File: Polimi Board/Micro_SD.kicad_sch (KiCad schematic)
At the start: 7 parts, among them J3 Micro_SD_Card, U4 74LVC125, U5 74LVC125

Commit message: Finish schematic part
To be reviewd
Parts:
- removed U5: 74LVC125, symbol 74xx:74LVC125
- added unit 2 of U4
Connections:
- net GND: now also U4.4; no longer J3.9 (SHIELD)
- net SCK_LLS: now also U4.6
- net at R8.2: now also U4.5
- new net Earth: J3.9 (SHIELD)

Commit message: Fatte modifiche
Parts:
- removed J3: Micro_SD_Card, symbol Connector:Micro_SD_Card
- removed U4: 74LVC125, symbol 74xx:74LVC125
- added J7: SD_Card, symbol Connector:SD_Card
- added R33, R34, R35: 47k, symbol Device:R
- R10, R7, R8, R9: value 3.3K -> 47k
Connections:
- net CS is gone; now on net +3.3V: R9.1
- net MISO is gone; now on net +3.3V: R10.1
- net MOSI is gone; now on net +3.3V: R7.1
- net SCK is gone; now on net +3.3V: R8.1
- net +3.3V: now also J7.4 (VDD), R33.1, R34.1, R35.1
- net GND: now also J7.12 (SHELL1), J7.13 (SHELL2), J7.3 (VSS), J7.6 (VSS)
- net SDMMC_D2: now reaches R7.2
- net SDMMC_D2: now also J7.9 (DAT2)
- net SDMMC_D0: now reaches R10.2
- net SDMMC_D0: now also J7.7 (DAT0)
- net SDMMC_D3: now reaches R8.2
- net SDMMC_D3: now also J7.1 (CD/DAT3)
- net SDMMC_CMD: now reaches R9.2
- net SDMMC_CMD: now also J7.2 (CMD)
- new net SDMMC_CD: J7.10 (CARD_DETECT), R34.2
- new net SDMMC_CK: J7.5 (CLK)
- new net SDMMC_D1: J7.8 (DAT1), R33.2
- new net SDMMC_WP: J7.11 (WRITE_PROTECT), R35.2
- no-connect marks 2 -> 0
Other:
- note removed: "Level shifter"

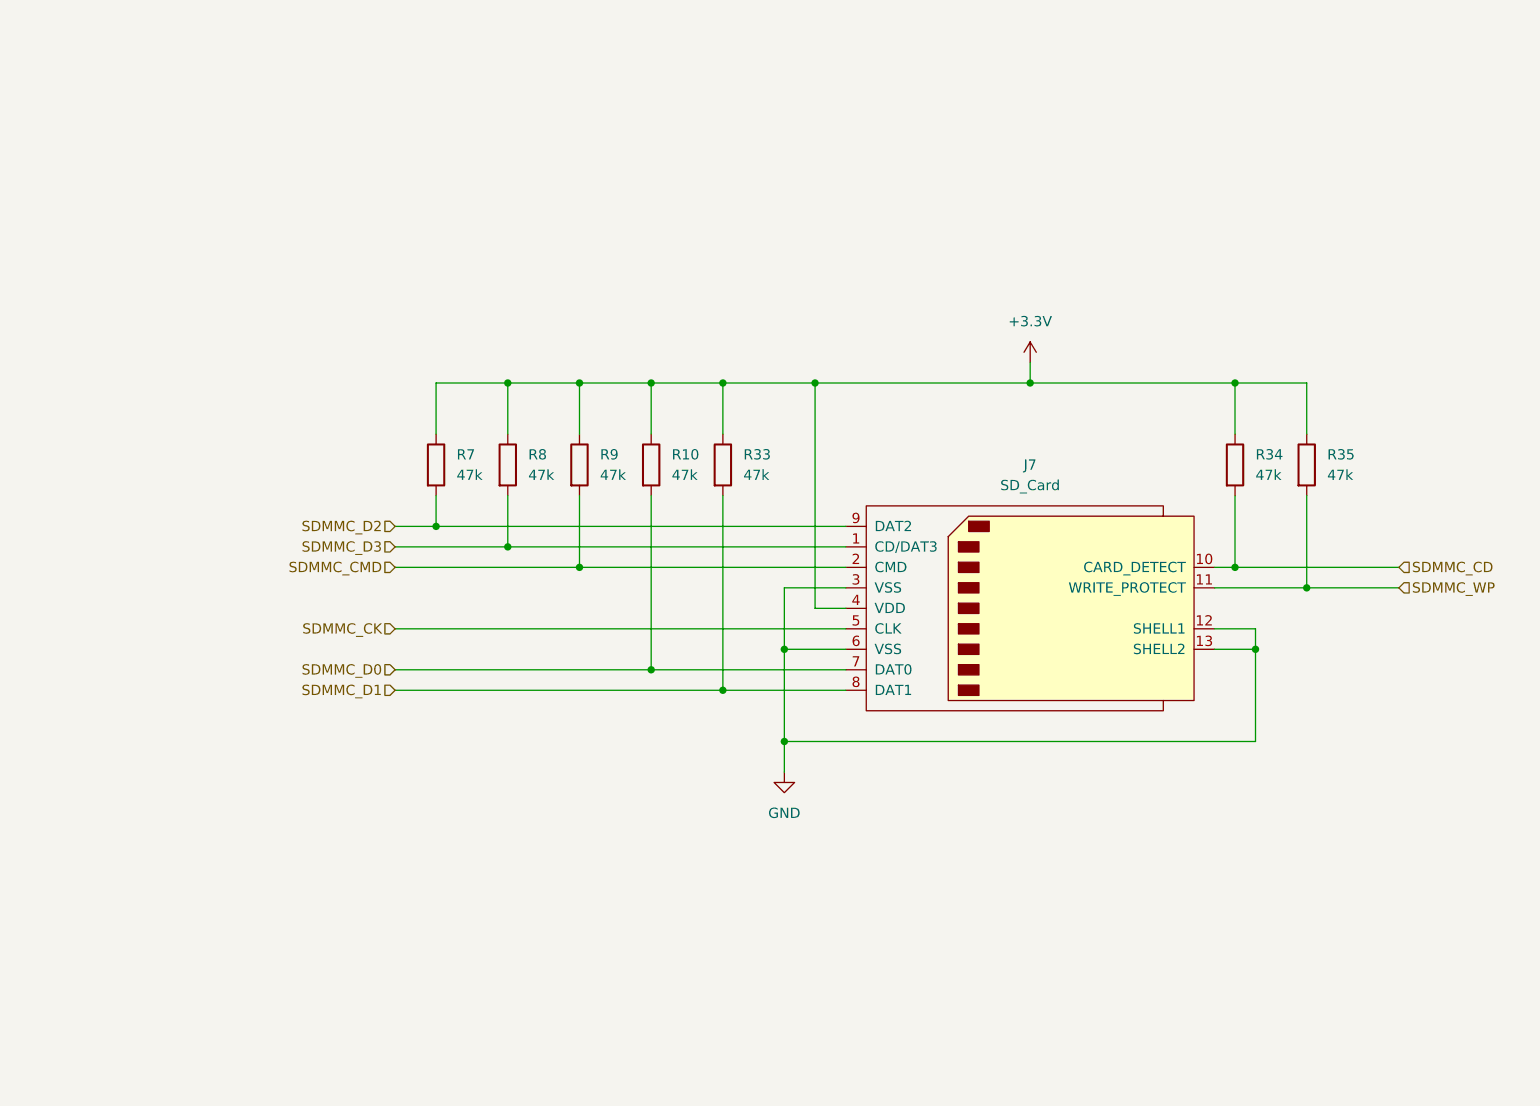
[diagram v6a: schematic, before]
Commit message: Added footprint from Mouser
readu for wiring
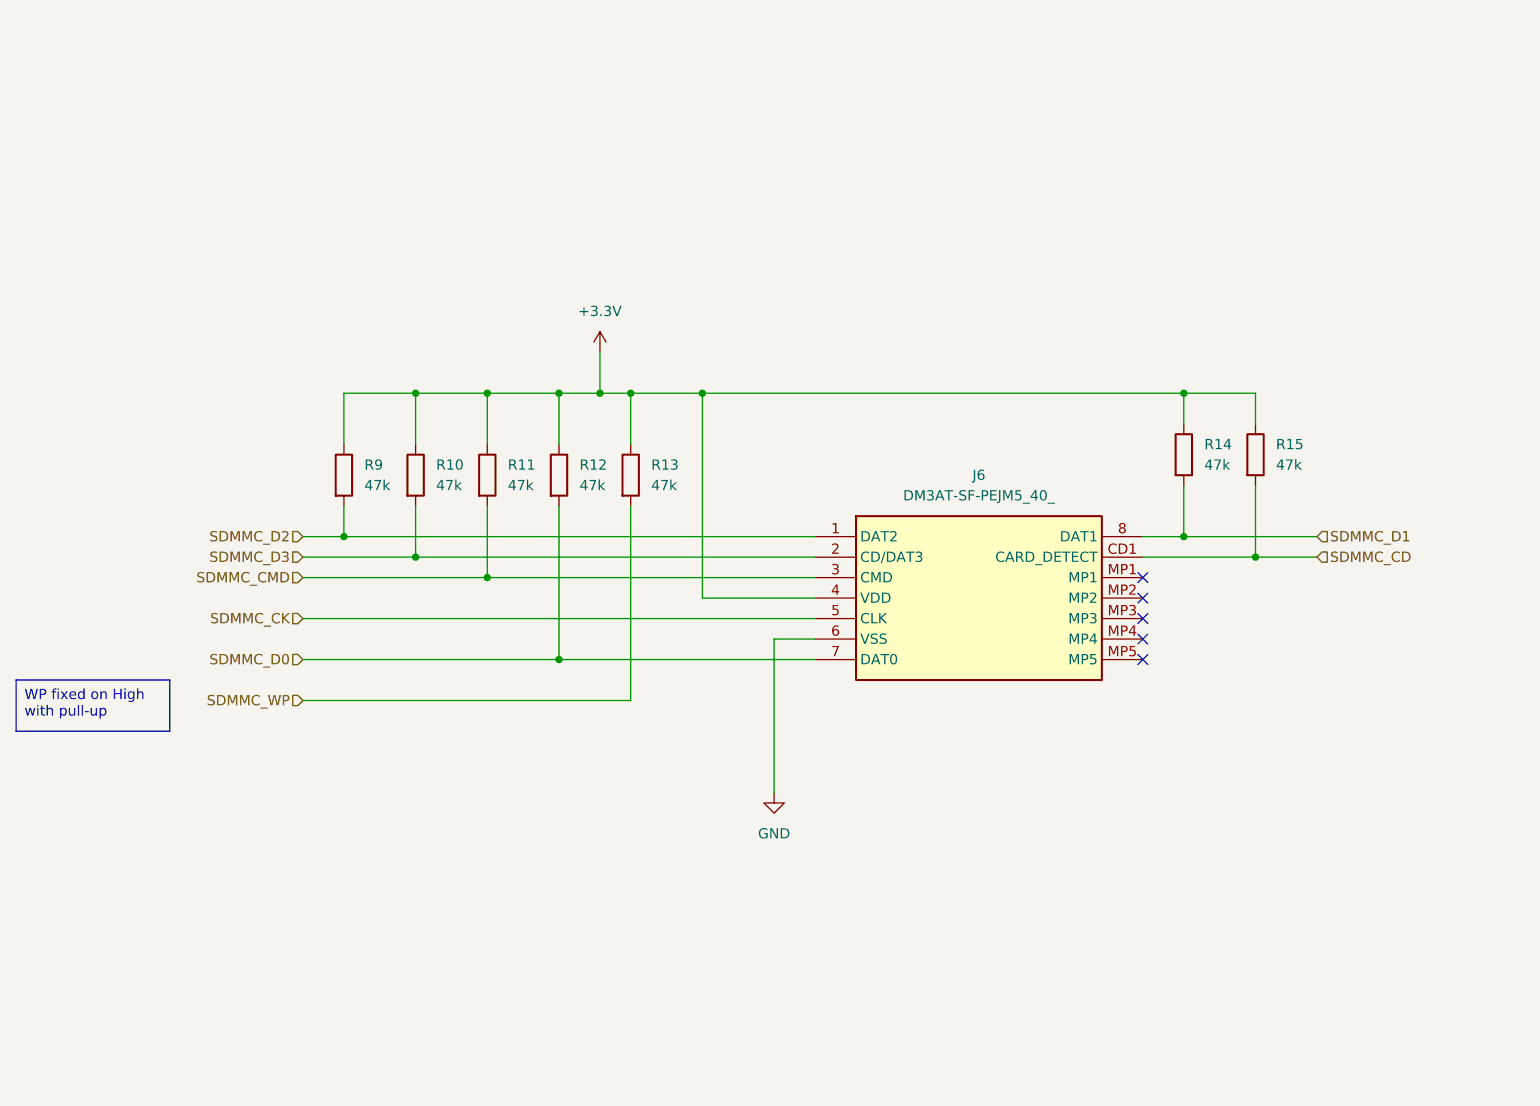
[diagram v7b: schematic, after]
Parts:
- removed J7: SD_Card, symbol Connector:SD_Card
- removed R33, R34, R35, R7, R8: 47k, symbol Device:R
- added J6: DM3AT-SF-PEJM5_40_, SamacSys_Parts:DM3ATSFPEJM540, symbol SamacSys_Parts:DM3AT-SF-PEJM5_40_
- added R11, R12, R13, R14, R15: 47k, Resistor_SMD:R_0603_1608Metric_Pad0.98x0.95mm_HandSolder, symbol Device:R
- R10, R9: footprint (none) -> Resistor_SMD:R_0603_1608Metric_Pad0.98x0.95mm_HandSolder
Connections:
- net +3.3V: now also J6.4 (VDD), R11.1, R12.1, R13.1, R14.1, R15.1
- net GND: now also J6.6 (VSS)
- net SDMMC_CD: now also J6.CD1 (CARD_DETECT), R15.2
- net SDMMC_CK: now also J6.5 (CLK)
- net SDMMC_CMD: now also J6.3 (CMD), R11.2; no longer R9.2
- net SDMMC_D0: now also J6.7 (DAT0), R12.2; no longer R10.2
- net SDMMC_D1: now also J6.8 (DAT1), R14.2
- net SDMMC_D2: now also R9.2, J6.1 (DAT2)
- net SDMMC_D3: now also R10.2, J6.2 (CD/DAT3)
- net SDMMC_WP: now also R13.2
- no-connect marks 0 -> 5

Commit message: PCB wip
before holidays
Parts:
- removed R13: 47k, Resistor_SMD:R_0603_1608Metric_Pad0.98x0.95mm_HandSolder, symbol Device:R
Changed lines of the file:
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@@
-	)
-	(junction
-		(at 124.46 66.04)
-		(diameter 0)
-		(color 0 0 0 0)
 	)
 	(junction
@@
 	(wire
 		(pts
-			(xy 124.46 104.14) (xy 83.82 104.14)
-		)
-		(stroke
-			(width 0)
-			(type default)
-		)
-	)
-	(wire
-		(pts
 			(xy 193.04 66.04) (xy 201.93 66.04)
 		)
@@
 	(wire
 		(pts
-			(xy 124.46 66.04) (xy 124.46 72.39)
-		)
-		(stroke
-			(width 0)
-			(type default)
-		)
-	)
-	(wire
-		(pts
-			(xy 124.46 66.04) (xy 133.35 66.04)
+			(xy 120.65 66.04) (xy 133.35 66.04)
 		)
 		(stroke
@@
 	(wire
 		(pts
-			(xy 147.32 96.52) (xy 142.24 96.52)
+			(xy 147.32 96.52) (xy 143.51 96.52)
 		)
 		(stroke
@@
 	(wire
 		(pts
-			(xy 124.46 80.01) (xy 124.46 104.14)
-		)
-		(stroke
-			(width 0)
-			(type default)
-		)
-	)
-	(wire
-		(pts
 			(xy 83.82 88.9) (xy 106.68 88.9)
 		)
@@
 	(wire
 		(pts
-			(xy 142.24 96.52) (xy 142.24 115.57)
+			(xy 143.51 96.52) (xy 143.51 104.14)
 		)
 		(stroke
@@
 	(wire
 		(pts
-			(xy 120.65 66.04) (xy 124.46 66.04)
-		)
-		(stroke
-			(width 0)
-			(type default)
-		)
-	)
-	(wire
-		(pts
 			(xy 120.65 66.04) (xy 120.65 60.96)
 		)
@@
 		)
 	)
-	(text_box "WP fixed on High with pull-up\n"
+	(text_box "WP not present in microSD\n\n"
 		(exclude_from_sim no)
-		(at 48.26 101.6 0)
+		(at 200.66 88.9 0)
 		(size 19.05 6.35)
 		(stroke
@@
 		)
 	)
-	(hierarchical_label "SDMMC_WP"
+	(hierarchical_label "SDMMC_CK"
 		(shape input)
-		(at 83.82 104.14 180)
+		(at 83.82 93.98 180)
 		(fields_autoplaced yes)
 		(effects
@@
 		)
 	)
-	(hierarchical_label "SDMMC_CK"
+	(hierarchical_label "SDMMC_CD"
 		(shape input)
-		(at 83.82 93.98 180)
+		(at 209.55 86.36 0)
 		(fields_autoplaced yes)
 		(effects
@@
 				(size 1.27 1.27)
 			)
-			(justify right)
-		)
-	)
-	(hierarchical_label "SDMMC_CD"
+			(justify left)
+		)
+	)
+	(hierarchical_label "SDMMC_D1"
 		(shape input)
-		(at 209.55 86.36 0)
+		(at 209.55 83.82 0)
 		(fields_autoplaced yes)
 		(effects
@@
 		)
 	)
-	(hierarchical_label "SDMMC_D1"
+	(hierarchical_label "SDMMC_CMD"
 		(shape input)
-		(at 209.55 83.82 0)
+		(at 83.82 88.9 180)
 		(fields_autoplaced yes)
 		(effects
@@
 				(size 1.27 1.27)
 			)
-			(justify left)
-		)
-	)
-	(hierarchical_label "SDMMC_CMD"
+			(justify right)
+		)
+	)
+	(hierarchical_label "SDMMC_D3"
 		(shape input)
-		(at 83.82 88.9 180)
+		(at 83.82 86.36 180)
 		(fields_autoplaced yes)
 		(effects
@@
 		)
 	)
-	(hierarchical_label "SDMMC_D3"
+	(hierarchical_label "SDMMC_D0"
 		(shape input)
-		(at 83.82 86.36 180)
+		(at 83.82 99.06 180)
 		(fields_autoplaced yes)
 		(effects
@@
 		)
 	)
-	(hierarchical_label "SDMMC_D0"
-		(shape input)
-		(at 83.82 99.06 180)
-		(fields_autoplaced yes)
-		(effects
-			(font
-				(size 1.27 1.27)
-			)
-			(justify right)
-		)
-	)
 	(symbol
 		(lib_id "power:GND")
-		(at 142.24 115.57 0)
+		(at 143.51 104.14 0)
 		(unit 1)
 		(exclude_from_sim no)
@@
 		(fields_autoplaced yes)
 		(property "Reference" "#PWR050"
-			(at 142.24 121.92 0)
+			(at 143.51 110.49 0)
 			(effects
 				(font
@@
 		)
 		(property "Value" "GND"
-			(at 142.24 120.65 0)
+			(at 143.51 109.22 0)
 			(effects
 				(font
@@
 		)
 		(property "Footprint" ""
-			(at 142.24 115.57 0)
+			(at 143.51 104.14 0)
 			(effects
 				(font
@@
 		)
 		(property "Datasheet" ""
-			(at 142.24 115.57 0)
+			(at 143.51 104.14 0)
 			(effects
 				(font
@@
 		)
 		(property "Description" ""
-			(at 142.24 115.57 0)
+			(at 143.51 104.14 0)
 			(effects
 				(font
@@
 					(unit 1)
 				)
-			)
-		)
-	)
-	(symbol
-		(lib_id "Device:R")
-		(at 124.46 76.2 0)
-		(unit 1)
-		(exclude_from_sim no)
-		(in_bom yes)
-		(on_board yes)
-		(dnp no)
-		(fields_autoplaced yes)
-		(property "Reference" "R13"
-			(at 127 74.93 0)
-			(effects
-				(font
-					(size 1.27 1.27)
-				)
-				(justify left)
-			)
-		)
-		(property "Value" "47k"
-			(at 127 77.47 0)
-			(effects
-				(font
-					(size 1.27 1.27)
-				)
-				(justify left)
-			)
-		)
-		(property "Footprint" "Resistor_SMD:R_0603_1608Metric_Pad0.98x0.95mm_HandSolder"
-			(at 122.682 76.2 90)
-			(effects
-				(font
-					(size 1.27 1.27)
-				)
-				(hide yes)
-			)
-		)
-		(property "Datasheet" "~"
-			(at 124.46 76.2 0)
-			(effects
-				(font
-					(size 1.27 1.27)
-				)
-				(hide yes)
-			)
-		)
-		(property "Description" ""
-			(at 124.46 76.2 0)
-			(effects
-				(font
-					(size 1.27 1.27)
-				)
-				(hide yes)
-			)
-		)
-		(pin "2"
-		)
-		(pin "1"
-		)
-		(instances
-			(project "Polimi Board"
-				(path "/319fe76e-1f98-44b3-99b0-af1a9ad7322c/58c63ef9-40c4-473e-87ef-db433b58ea6c"
-					(reference "R13")
-					(unit 1)
-				)
